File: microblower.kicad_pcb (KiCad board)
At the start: 2 copper layers, 18 parts, among them Q1 2N7000, U1 NE555P, U2 L293D, U3 LM78L05_TO92, U4 TL072

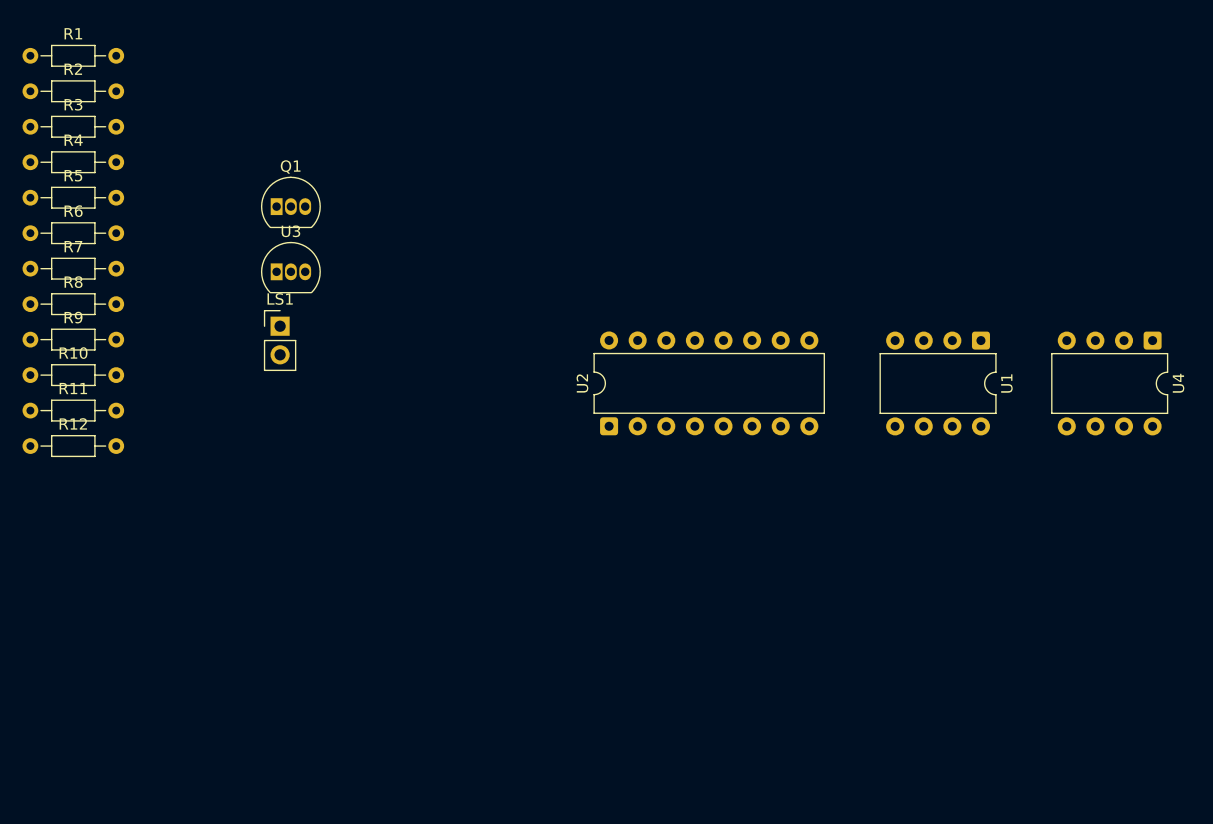
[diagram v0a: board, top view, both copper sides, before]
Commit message: Tried basic pierce oscillator
Didn't have enough phase shift
I think the feedback resistor is misplaced
No way to drive the second side of the invertere
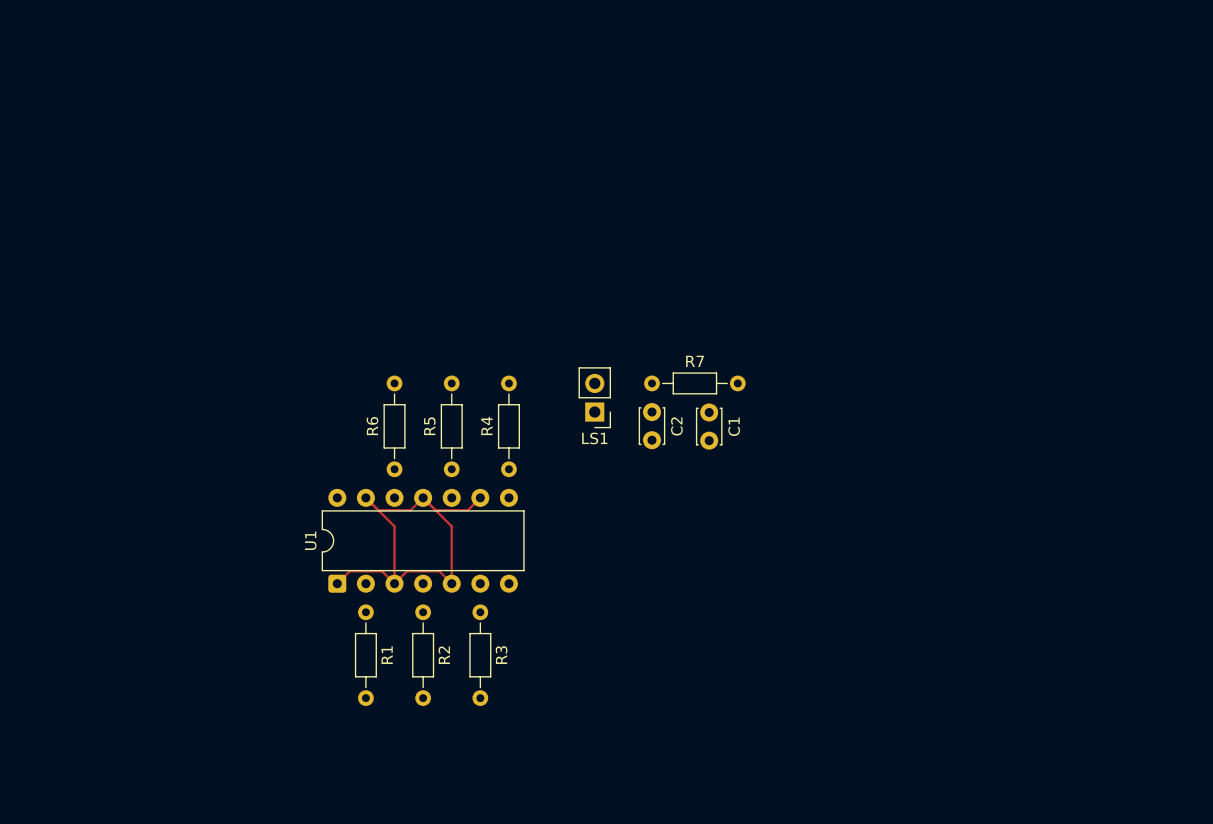
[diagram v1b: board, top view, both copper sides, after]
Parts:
- removed Q1: 2N7000, Package_TO_SOT_THT:TO-92_Inline
- removed R10, R11, R12, R9: 10k, Resistor_THT:R_Axial_DIN0204_L3.6mm_D1.6mm_P7.62mm_Horizontal
- removed R8: 100k, Resistor_THT:R_Axial_DIN0204_L3.6mm_D1.6mm_P7.62mm_Horizontal
- removed U2: L293D, Package_DIP:DIP-16_W7.62mm
- removed U3: LM78L05_TO92, Package_TO_SOT_THT:TO-92_Inline
- removed U4: TL072, Package_DIP:DIP-8_W7.62mm
- added C1: 1n, Capacitor_THT:C_Disc_D3.0mm_W2.0mm_P2.50mm, F.Cu at (91.4, 58.5)
- added C2: 1n, Capacitor_THT:C_Disc_D3.0mm_W2.0mm_P2.50mm, F.Cu at (86.4, 58.4)
- R1, R2: value 10 -> 100
- R3, R4, R5, R6: value 10k -> 100
- R7: value 100k -> 1k
- U1: value NE555P -> 4069; footprint Package_DIP:DIP-8_W7.62mm -> Package_DIP:DIP-14_W7.62mm
- moved U1 61.1 mm to (58.4, 73.7), turned to 90 degrees
- moved R3 58.8 mm to (71.1, 76.2), turned to -90 degrees
- moved R2 57.9 mm to (66.0, 76.2), turned to -90 degrees
- moved R1 57.7 mm to (61.0, 76.2), turned to -90 degrees
- moved R7 56.1 mm to (86.4, 55.9)
- moved R4 50.5 mm to (73.7, 63.5), turned to 90 degrees
- moved R5 44.5 mm to (68.6, 63.5), turned to 90 degrees
- moved R6 38.5 mm to (63.5, 63.5), turned to 90 degrees
- moved LS1 29.0 mm to (81.3, 58.4), turned to 180 degrees
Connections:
- LS1 pad 1: Net-(LS1-Pad1) -> Net-(C2-Pad1)
- LS1 pad 2: Net-(LS1-Pad2) -> Net-(C1-Pad1)
- R1 pad 1: Net-(U2-1Y) -> Net-(R1-Pad1)
- R1 pad 2: Net-(LS1-Pad1) -> Net-(C1-Pad1)
- R2 pad 1: Net-(U2-2Y) -> Net-(R2-Pad1)
- R2 pad 2: Net-(LS1-Pad2) -> Net-(C1-Pad1)
- R3 pad 1: +5V -> Net-(R3-Pad1)
- R3 pad 2: Net-(Q1-D) -> Net-(C1-Pad1)
- R4 pad 1: +5V -> Net-(R4-Pad1)
- R4 pad 2: Net-(Q1-G) -> Net-(C1-Pad1)
- R5 pad 1: Net-(LS1-Pad2) -> Net-(R5-Pad1)
- R5 pad 2: Net-(U4A--) -> Net-(C1-Pad1)
- R6 pad 1: Net-(U2-2Y) -> Net-(R6-Pad1)
- R6 pad 2: Net-(U4A-+) -> Net-(C1-Pad1)
- R7 pad 1: Net-(U4A-+) -> Net-(C2-Pad1)
- R7 pad 2: Net-(U4B--) -> Net-(C1-Pad1)
- U1 pad 1: GND -> Net-(C2-Pad1)
- U1 pad 2: /TRIGGER -> Net-(R1-Pad1)
- U1 pad 3: Net-(U1-Q) -> Net-(C2-Pad1)
- U1 pad 4: +5V -> Net-(R2-Pad1)
- U1 pad 5: unconnected-(U1-CV-Pad5) -> Net-(C2-Pad1)
- U1 pad 6: /TRIGGER -> Net-(R3-Pad1)
- U1 pad 7: Net-(Q1-G) -> GND
- U1 pad 8: +12V -> Net-(R4-Pad1)
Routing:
- net Net-(C2-Pad1): track 0.00 -> 41.3 mm

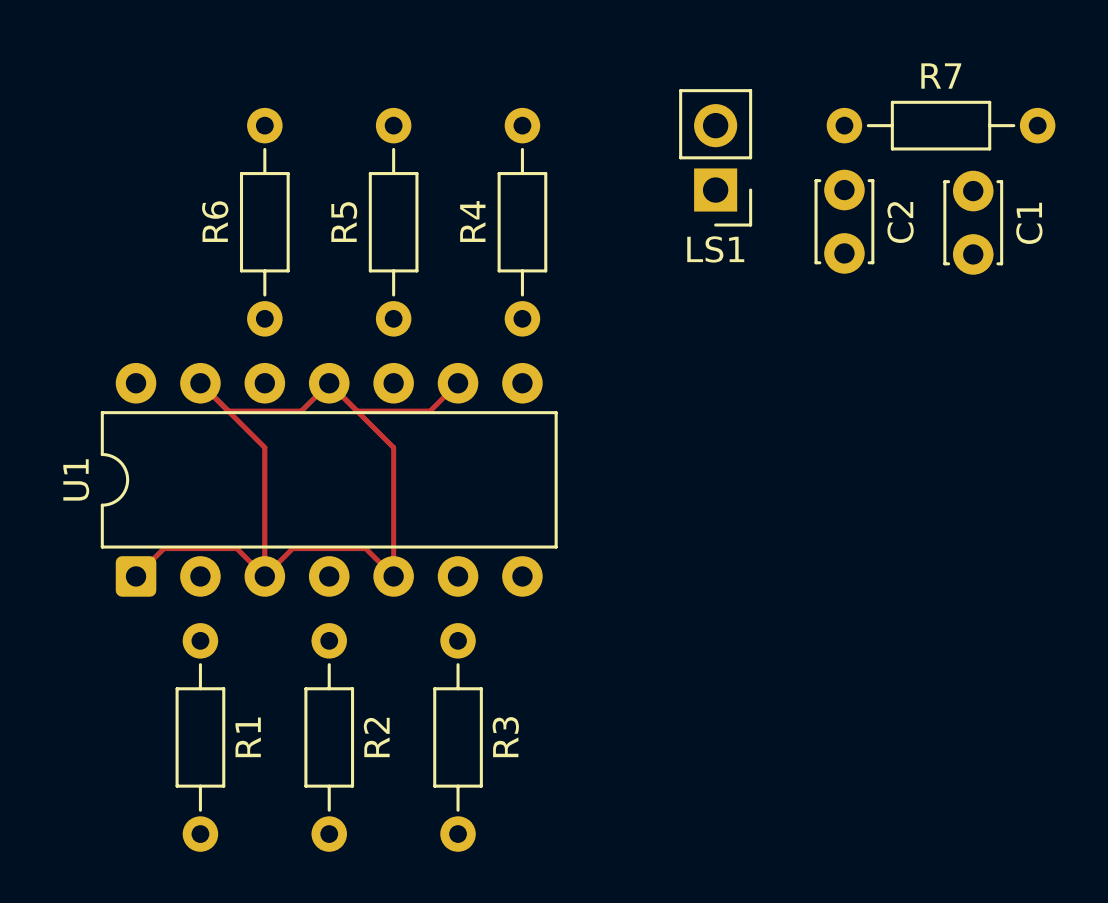
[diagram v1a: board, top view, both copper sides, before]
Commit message: Switched to relaxation oscillator
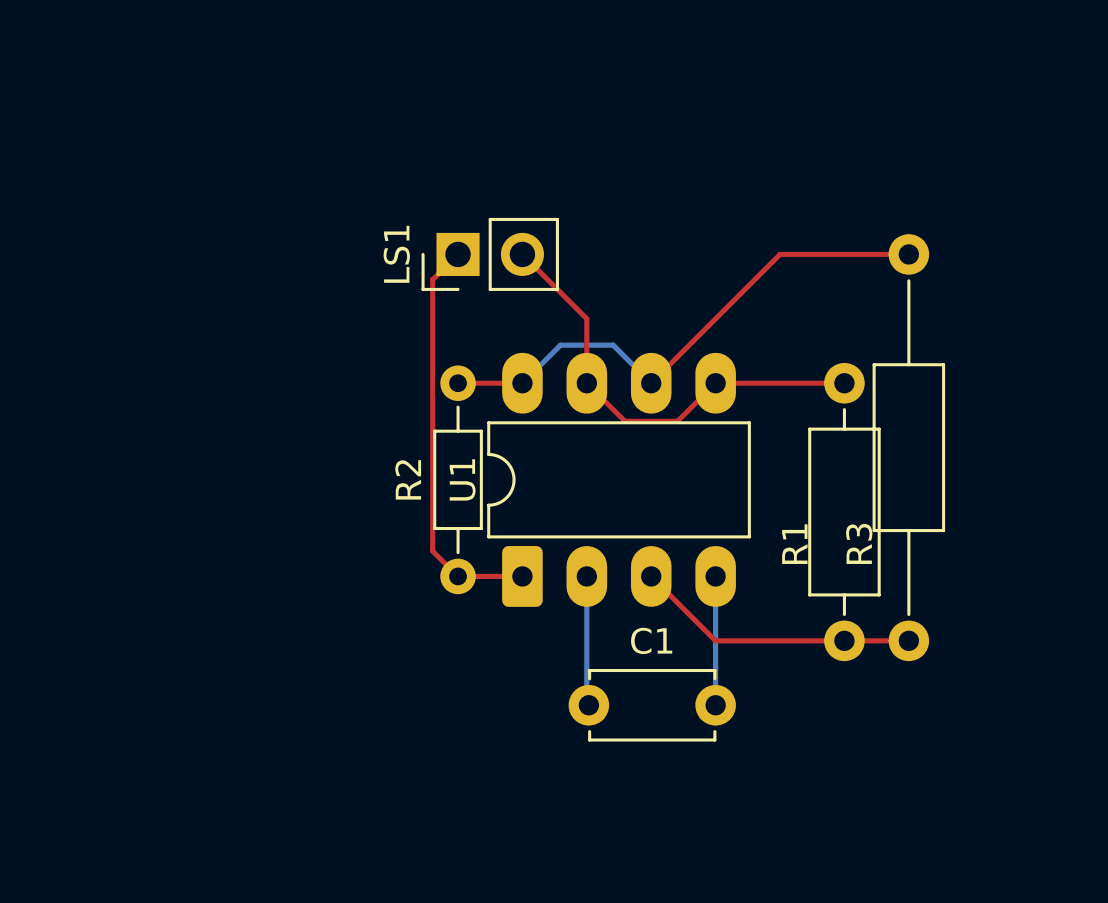
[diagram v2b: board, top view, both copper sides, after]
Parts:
- removed C2: 1n, Capacitor_THT:C_Disc_D3.0mm_W2.0mm_P2.50mm
- removed R4, R5, R6: 100, Resistor_THT:R_Axial_DIN0204_L3.6mm_D1.6mm_P7.62mm_Horizontal
- removed R7: 1k, Resistor_THT:R_Axial_DIN0204_L3.6mm_D1.6mm_P7.62mm_Horizontal
- C1: value 1n -> 1u; footprint Capacitor_THT:C_Disc_D3.0mm_W2.0mm_P2.50mm -> Capacitor_THT:C_Disc_D4.7mm_W2.5mm_P5.00mm
- LS1: value Speaker_Crystal -> microblower
- R1: value 100 -> 10; footprint Resistor_THT:R_Axial_DIN0204_L3.6mm_D1.6mm_P7.62mm_Horizontal -> Resistor_THT:R_Axial_DIN0207_L6.3mm_D2.5mm_P10.16mm_Horizontal
- R2: value 100 -> 10k
- R3: value 100 -> 1k; footprint Resistor_THT:R_Axial_DIN0204_L3.6mm_D1.6mm_P7.62mm_Horizontal -> Resistor_THT:R_Axial_DIN0207_L6.3mm_D2.5mm_P15.24mm_Horizontal
- U1: value 4069 -> L272M; footprint Package_DIP:DIP-14_W7.62mm -> Package_DIP:DIP-8_W7.62mm_LongPads
- moved R1 25.4 mm to (86.4, 76.2), turned to 90 degrees
- moved C1 25.3 mm to (76.3, 78.7), turned to 0 degrees
- moved R3 17.8 mm to (88.9, 76.2), turned to 90 degrees
- moved U1 15.2 mm to (73.7, 73.7)
- moved LS1 10.5 mm to (71.1, 61.0), turned to 90 degrees
- moved R2 5.68 mm to (71.1, 73.7), turned to 90 degrees
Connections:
- C1 pad 1: Net-(C1-Pad1) -> +12V
- LS1 pad 1: Net-(C2-Pad1) -> Net-(LS1-Pad1)
- LS1 pad 2: Net-(C1-Pad1) -> Net-(U1A-+)
- R1 pad 2: Net-(C1-Pad1) -> Net-(U1A-+)
- R2 pad 1: Net-(R2-Pad1) -> Net-(LS1-Pad1)
- R2 pad 2: Net-(C1-Pad1) -> Net-(U1A--)
- R3 pad 1: Net-(R3-Pad1) -> Net-(R1-Pad1)
- R3 pad 2: Net-(C1-Pad1) -> Net-(U1A--)
- U1 pad 1: Net-(C2-Pad1) -> Net-(LS1-Pad1)
- U1 pad 2: Net-(R1-Pad1) -> +12V
- U1 pad 3: Net-(C2-Pad1) -> Net-(R1-Pad1)
- U1 pad 4: Net-(R2-Pad1) -> GND
- U1 pad 5: Net-(C2-Pad1) -> Net-(U1A-+)
- U1 pad 6: Net-(R3-Pad1) -> Net-(U1A--)
- U1 pad 7: GND -> Net-(U1A-+)
- U1 pad 8: Net-(R4-Pad1) -> Net-(U1A--)
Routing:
- net Net-(C2-Pad1): track 41.3 -> 0.00 mm
- net Net-(U1A--): track 0.00 -> 21.1 mm
- net Net-(U1A-+): track 0.00 -> 17.5 mm
- net Net-(LS1-Pad1): track 0.00 -> 16.1 mm
- net Net-(R1-Pad1): track 0.00 -> 11.2 mm
- net +12V: track 0.00 -> 5.11 mm
- net GND: track 0.00 -> 5.08 mm

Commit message: Settled on design for microblower
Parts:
- removed R3: 1k, Resistor_THT:R_Axial_DIN0207_L6.3mm_D2.5mm_P15.24mm_Horizontal
- added C2: 1u, Capacitor_THT:C_Disc_D4.7mm_W2.5mm_P5.00mm, F.Cu at (76.2, 88.9)
- added C3: 1u, Capacitor_THT:C_Disc_D4.7mm_W2.5mm_P5.00mm, F.Cu at (96.5, 71.0)
- added Q1: 2N7000, Package_TO_SOT_THT:TO-92L_Inline_Wide, F.Cu at (91.4, 63.0)
- added RV1: 5k, Potentiometer_THT:Potentiometer_Bourns_3266Y_Vertical, F.Cu at (114.3, 86.4)
- added U2: L293, Package_DIP:DIP-16_W7.62mm, F.Cu at (58.4, 83.8)
- added U3: L78L05_TO92, Package_TO_SOT_THT:TO-92L_Inline_Wide, F.Cu at (96.5, 73.7)
- C1: value 1u -> 1n
- R1: value 10 -> 10k; footprint Resistor_THT:R_Axial_DIN0207_L6.3mm_D2.5mm_P10.16mm_Horizontal -> Resistor_THT:R_Axial_DIN0207_L6.3mm_D2.5mm_P2.54mm_Vertical
- R2: footprint Resistor_THT:R_Axial_DIN0204_L3.6mm_D1.6mm_P7.62mm_Horizontal -> Resistor_THT:R_Axial_DIN0207_L6.3mm_D2.5mm_P2.54mm_Vertical
- U1: value L272M -> NE555P; footprint Package_DIP:DIP-8_W7.62mm_LongPads -> Package_DIP:DIP-8_W7.62mm
- moved U1 25.0 mm to (96.5, 83.8)
- moved C1 24.0 mm to (99.1, 86.4), turned to -90 degrees
- moved R2 13.0 mm to (58.4, 71.1), turned to 0 degrees
- moved R1 11.4 mm to (76.2, 71.1), turned to 180 degrees
- moved LS1 3.59 mm to (68.6, 63.5), turned to -90 degrees
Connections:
- C1 pad 1: +12V -> Net-(U1-THR)
- LS1 pad 1: Net-(LS1-Pad1) -> Net-(U2-3Y)
- LS1 pad 2: Net-(U1A-+) -> Net-(U2-4Y)
- R1 pad 1: Net-(R1-Pad1) -> +5V
- R1 pad 2: Net-(U1A-+) -> Net-(Q1-G)
- R2 pad 1: Net-(LS1-Pad1) -> +5V
- R2 pad 2: Net-(U1A--) -> Net-(Q1-D)
- U1 pad 1: Net-(LS1-Pad1) -> GND
- U1 pad 2: +12V -> Net-(U1-THR)
- U1 pad 3: Net-(R1-Pad1) -> Net-(U1-Q)
- U1 pad 4: GND -> +5V
- U1 pad 5: Net-(U1A-+) -> unconnected-(U1-CV-Pad5)
- U1 pad 6: Net-(U1A--) -> Net-(U1-THR)
- U1 pad 7: Net-(U1A-+) -> Net-(Q1-G)
- U1 pad 8: Net-(U1A--) -> +5V
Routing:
- net GND: track 5.08 -> 92.4 mm
- net +5V: track 0.00 -> 80.2 mm
- net Net-(Q1-G): track 0.00 -> 49.0 mm
- net Net-(Q1-D): track 0.00 -> 34.8 mm
- net Net-(U1-THR): track 0.00 -> 23.9 mm
- net Net-(U1A--): track 21.1 -> 0.00 mm
- net Net-(U1A-+): track 17.5 -> 0.00 mm
- net Net-(LS1-Pad1): track 16.1 -> 0.00 mm
- net Net-(U2-4Y): track 0.00 -> 13.8 mm
- net Net-(U2-3Y): track 0.00 -> 13.8 mm
- net Net-(U1-Q): track 0.00 -> 13.8 mm
- net Net-(R1-Pad1): track 11.2 -> 0.00 mm
- net +12V: track 5.11 -> 8.89 mm, vias 0 -> 1
